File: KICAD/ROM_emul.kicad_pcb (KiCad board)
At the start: 2 copper layers, 94 x 53.3 mm, 15 parts, among them U1 HM62256BLFP-7ULT, U2 74LS541, U3 74LS541, U4 74LS541, U5 27C256Socket

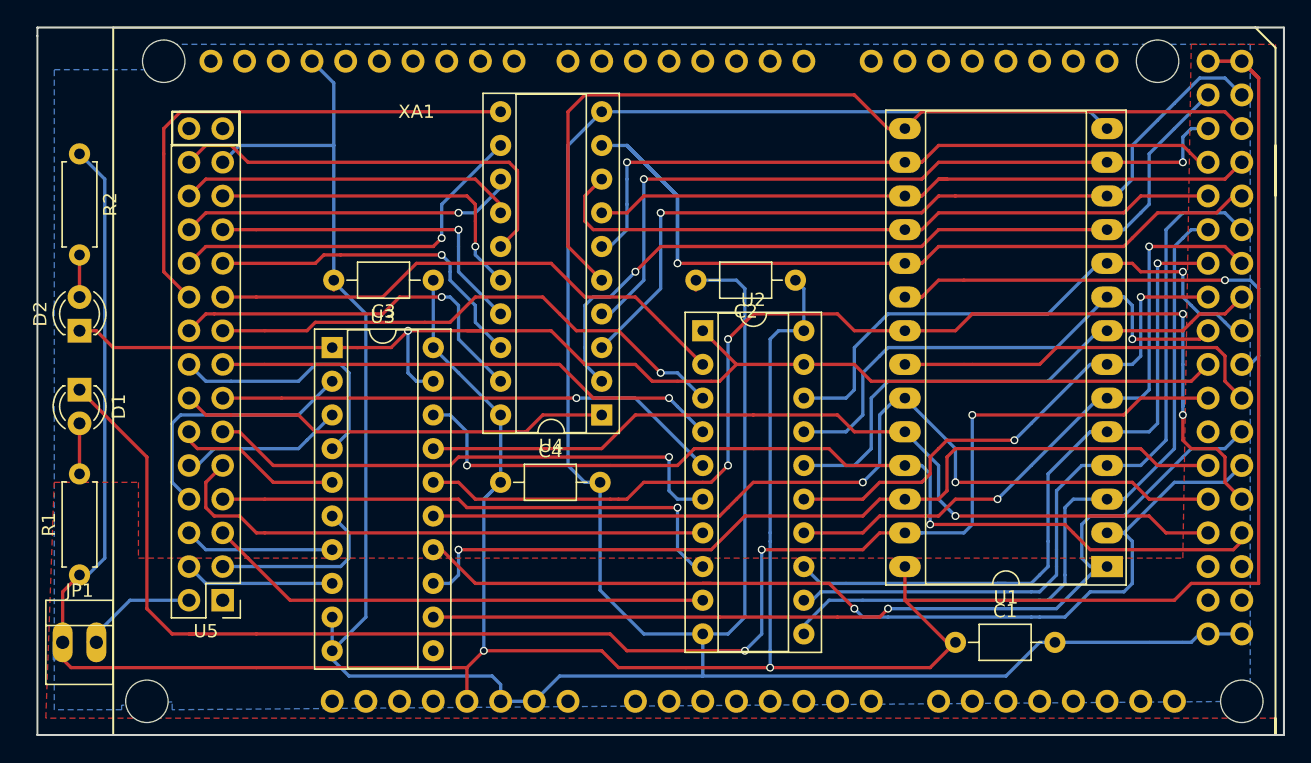
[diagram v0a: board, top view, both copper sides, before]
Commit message: PCB Correction to avoid USB Connector Overlap
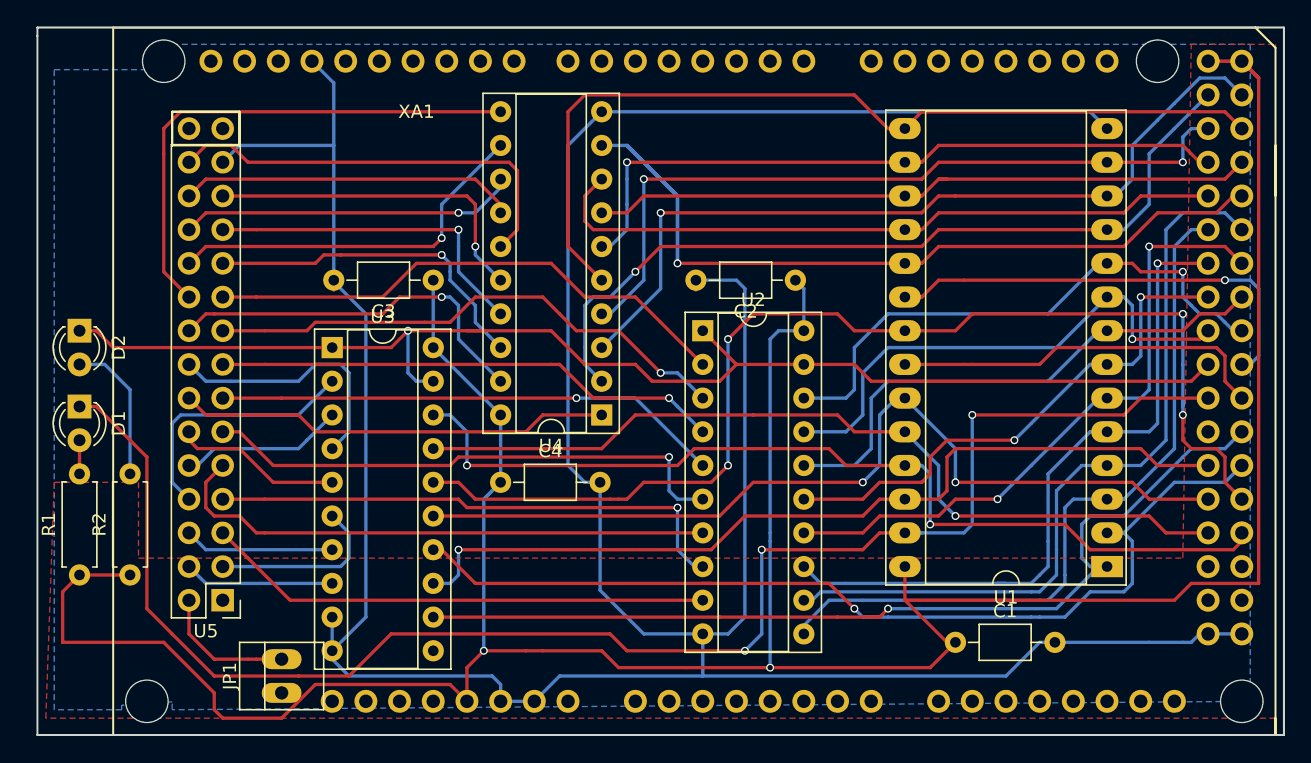
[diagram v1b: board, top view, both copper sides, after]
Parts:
- moved R2 32.0 mm to (115.6, 133.3), turned to 90 degrees
- moved JP1 16.9 mm to (127.0, 142.2), turned to 90 degrees
- moved D1 1.27 mm to (111.8, 120.7)
- turned D2 to 270 degrees
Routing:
- net VCC: track 263.3 -> 235.8 mm
- net Net-(D2-Pad2): track 3.17 -> 10.9 mm
- net Net-(D1-Pad1): track 117.7 -> 119.1 mm
- net Net-(JP1-Pad2): track 8.94 -> 10.3 mm
- net Net-(D1-Pad2): track 3.81 -> 2.54 mm
